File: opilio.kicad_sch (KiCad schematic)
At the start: 87 parts, among them J1 Screw_Terminal_01x02, J2 USB_B_Micro, J3 Conn_01x02_Male, J4 Conn_01x02_Male, J5 Conn_01x02_Male, Q1 PMV25ENEAR, U1 EUP3458, U2 STM32F103C8T6, Y1 YSX531SL 8MHz, Y2 YST310S 32.768KHz

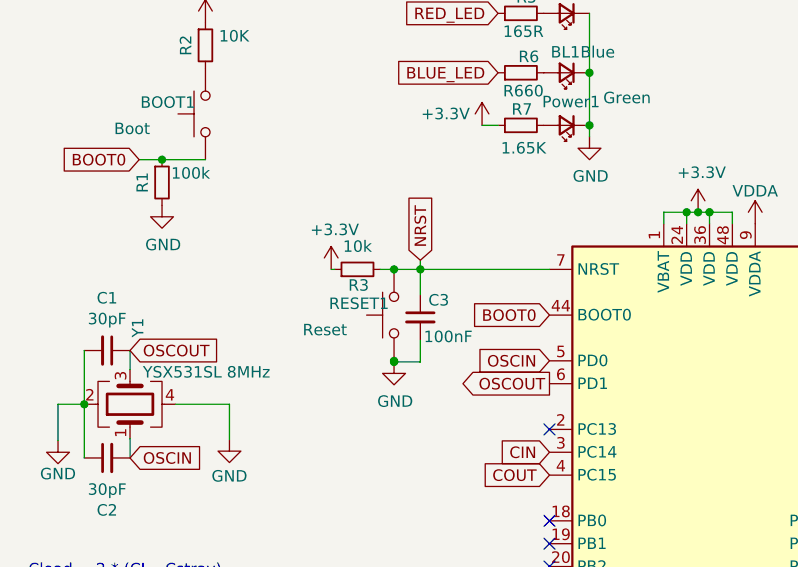
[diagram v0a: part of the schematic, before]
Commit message: bigger pads for mosfets
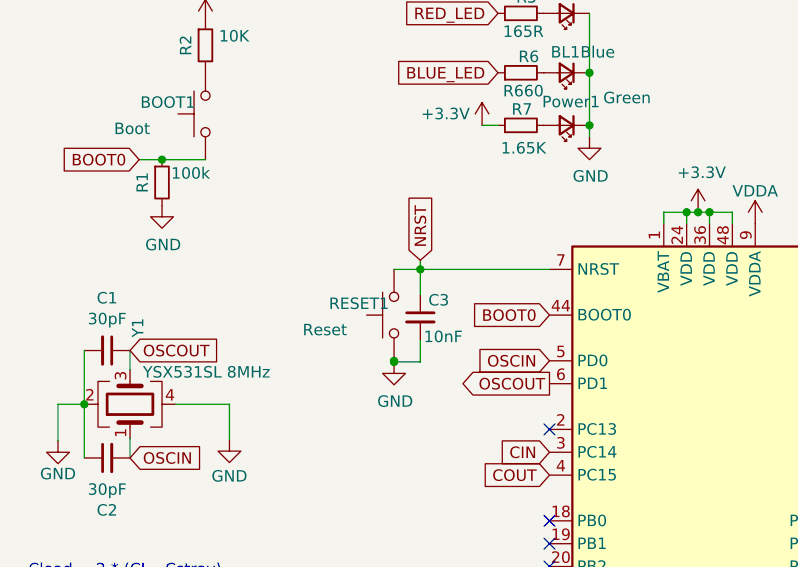
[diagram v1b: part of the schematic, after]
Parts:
- removed R3: 10k, Resistor_SMD:R_0603_1608Metric_Pad0.98x0.95mm_HandSolder, symbol Device:R_Small
- C3: value 100nF -> 10nF
- Q1: footprint easyeda2kicad:SOT-23_L2.9-W1.3-P1.90-LS2.4-BR -> Package_TO_SOT_SMD:SOT-23
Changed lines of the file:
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@@
   (junction (at 88.773 112.522) (diameter 0) (color 0 0 0 0)
   )
-  (junction (at 53.721 118.872) (diameter 0) (color 0 0 0 0)
-  )
   (junction (at 17.907 166.37) (diameter 0) (color 0 0 0 0)
   )
@@
     (stroke (width 0) (type default) (color 0 0 0 0))
   )
-  (wire (pts (xy 52.197 118.872) (xy 53.721 118.872))
-    (stroke (width 0) (type default) (color 0 0 0 0))
-  )
   (wire (pts (xy 14.732 27.178) (xy 14.732 31.75))
     (stroke (width 0) (type default) (color 0 0 0 0))
@@
     (stroke (width 0) (type default) (color 0 0 0 0))
   )
-  (wire (pts (xy 46.736 118.872) (xy 47.117 118.872))
-    (stroke (width 0) (type default) (color 0 0 0 0))
-  )
   (wire (pts (xy 221.996 101.092) (xy 219.456 101.092))
     (stroke (width 0) (type default) (color 0 0 0 0))
@@
     )
   )
-  (symbol (lib_id "Device:R_Small") (at 49.657 118.872 90) (unit 1)
-    (in_bom yes) (on_board yes)
-    (property "Reference" "R3" (id 0) (at 49.784 120.65 90))
-    (property "Value" "10k" (id 1) (at 49.657 116.332 90))
-    (property "Footprint" "Resistor_SMD:R_0603_1608Metric_Pad0.98x0.95mm_HandSolder" (id 2) (at 49.657 118.872 0)
-      (effects (font (size 1.27 1.27)) hide)
-    )
-    (property "Datasheet" "~" (id 3) (at 49.657 118.872 0)
-      (effects (font (size 1.27 1.27)) hide)
-    )
-    (pin "1")
-    (pin "2")
-  )
   (symbol (lib_id "Switch:SW_Push") (at 32.766 101.6 90) (unit 1)
     (in_bom yes) (on_board yes)
@@
       (effects (font (size 1.27 1.27)) (justify left))
     )
-    (property "Value" "100nF" (id 1) (at 57.023 126.365 0)
+    (property "Value" "10nF" (id 1) (at 57.023 126.365 0)
       (effects (font (size 1.27 1.27)) (justify left))
     )
@@
       (effects (font (size 1.27 1.27)) (justify left))
     )
-    (property "Footprint" "easyeda2kicad:SOT-23_L2.9-W1.3-P1.90-LS2.4-BR" (id 2) (at 204.343 91.44 0)
+    (property "Footprint" "Package_TO_SOT_SMD:SOT-23" (id 2) (at 204.343 91.44 0)
       (effects (font (size 1.27 1.27)) hide)
     )
@@
     (pin "1")
   )
-  (symbol (lib_id "power:+3.3V") (at 46.736 118.872 0) (unit 1)
-    (in_bom yes) (on_board yes)
-    (property "Reference" "#PWR09" (id 0) (at 46.736 122.682 0)
-      (effects (font (size 1.27 1.27)) hide)
-    )
-    (property "Value" "+3.3V" (id 1) (at 47.117 114.4778 0))
-    (property "Footprint" "" (id 2) (at 46.736 118.872 0)
-      (effects (font (size 1.27 1.27)) hide)
-    )
-    (property "Datasheet" "" (id 3) (at 46.736 118.872 0)
-      (effects (font (size 1.27 1.27)) hide)
-    )
-    (pin "1")
-  )
   (symbol (lib_id "power:GND") (at 87.503 192.532 0) (unit 1)
     (in_bom yes) (on_board yes)
@@
       (reference "#PWR08") (unit 1) (value "GND") (footprint "")
     )
-    (path "/fcdd5368-7d46-4e3b-b033-9204303556cd"
-      (reference "#PWR09") (unit 1) (value "+3.3V") (footprint "")
-    )
     (path "/53efbcf9-b8b0-41cf-b5f1-95d5ffb0f13b"
       (reference "#PWR010") (unit 1) (value "+12V") (footprint "")
@@
     )
     (path "/725ad605-0047-4399-a661-42b9902e5238"
-      (reference "C3") (unit 1) (value "100nF") (footprint "Capacitor_SMD:C_0603_1608Metric_Pad1.08x0.95mm_HandSolder")
+      (reference "C3") (unit 1) (value "10nF") (footprint "Capacitor_SMD:C_0603_1608Metric_Pad1.08x0.95mm_HandSolder")
     )
     (path "/9d3abc30-14c9-40c1-8ddc-4b7be6965203"
@@
     )
     (path "/df940eb1-429e-48e8-8206-0d27bc3ed7bd"
-      (reference "Q1") (unit 1) (value "PMV25ENEAR") (footprint "easyeda2kicad:SOT-23_L2.9-W1.3-P1.90-LS2.4-BR")
+      (reference "Q1") (unit 1) (value "PMV25ENEAR") (footprint "Package_TO_SOT_SMD:SOT-23")
     )
     (path "/be987873-4856-4ad7-aaee-745ffdc5e733"
@@
       (reference "R2") (unit 1) (value "10K") (footprint "Resistor_SMD:R_0603_1608Metric_Pad0.98x0.95mm_HandSolder")
     )
-    (path "/058aa005-48f2-4086-a77a-42a9c22cdeee"
-      (reference "R3") (unit 1) (value "10k") (footprint "Resistor_SMD:R_0603_1608Metric_Pad0.98x0.95mm_HandSolder")
-    )
     (path "/beb113ce-d7fe-47cb-97e6-be05f9ef150e"

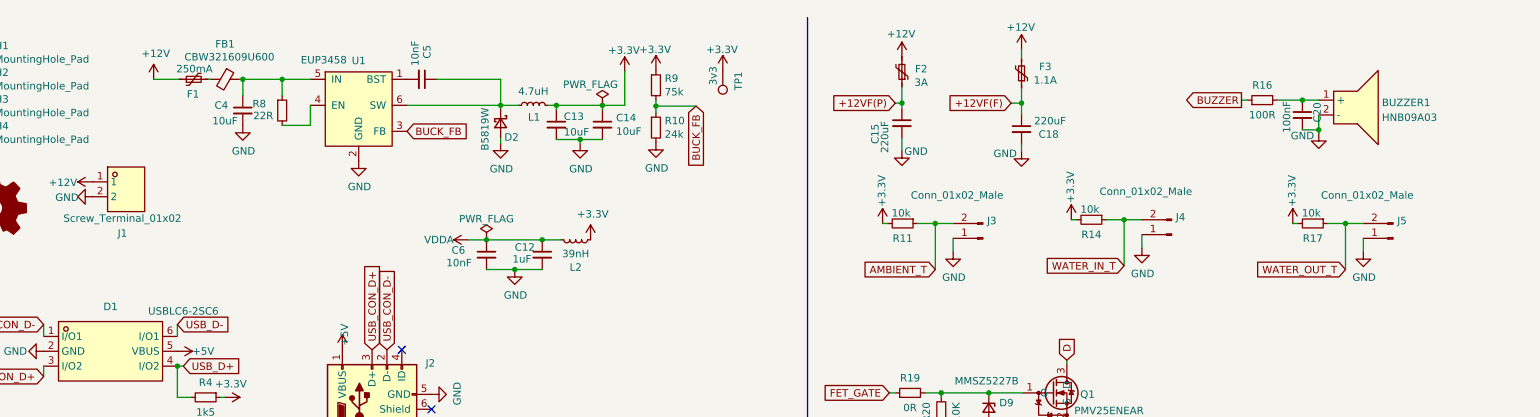
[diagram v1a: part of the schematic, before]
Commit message: added 3d models
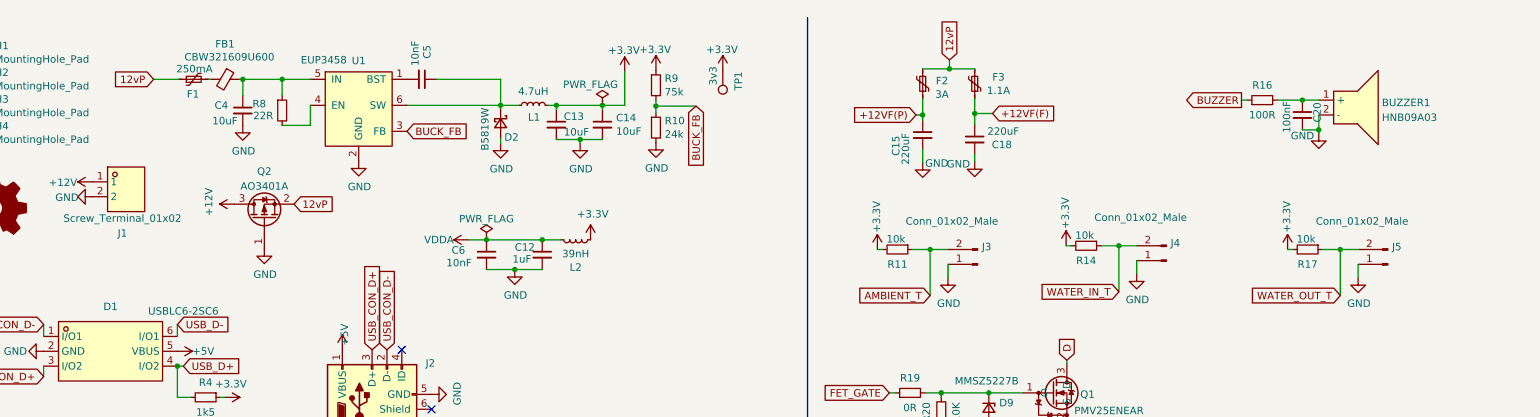
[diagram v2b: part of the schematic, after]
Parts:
- added Q2: AO3401A, Package_TO_SOT_SMD:SOT-23, symbol Transistor_FET:AO3401A
- D1: footprint easyeda2kicad:SOT-666-6_L1.6-W1.2-P0.50-LS1.6-BL -> Package_TO_SOT_SMD:SOT-666
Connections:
- net +12V: now also Q2.3 (D); no longer F1.1, F2.2, F3.2
- net GND: now also Q2.1 (G)
- new net 12vP: F1.1, F2.2, F3.2, Q2.2 (S)
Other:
- moved on the sheet: C15, C18, F2, F3, J3, J4, J5, R11, R14, R17

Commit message: cleanup and annotate schema
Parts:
- F2: value 3A -> 2A; footprint Fuse:Fuse_1812_4532Metric_Pad1.30x3.40mm_HandSolder -> Fuse:Fuse_1206_3216Metric_Pad1.42x1.75mm_HandSolder
- R20: value 10K -> 7k5
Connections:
- net USB_CON_D+: now also R4.2
- net USB_D+: no longer R4.2
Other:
- note added: "10k Thermistor Input"
- note added: "Audio/Visual Output"
- note added: "ESD Protection"
- note added: "MCU"
- note added: "N-FET"
- note added: "Power"
- note added: "Power Output"
- moved on the sheet: BL1, BUZZER1, C10, C11, C12, C15, C18, C20, C6, C7, C8, C9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

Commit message: WIP:0402
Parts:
- C1, C10, C11, C16, C17, C19, C2, C20, C21, C22, C23, C3, C6, C8, C9: footprint Capacitor_SMD:C_0603_1608Metric_Pad1.08x0.95mm_HandSolder -> Capacitor_SMD:C_0402_1005Metric_Pad0.74x0.62mm_HandSolder
- R1, R10, R11, R12, R13, R14, R15, R16, R17, R18, R2, R20, R4, R5, R6, R7, R8, R9: footprint Resistor_SMD:R_0603_1608Metric_Pad0.98x0.95mm_HandSolder -> Resistor_SMD:R_0402_1005Metric_Pad0.72x0.64mm_HandSolder

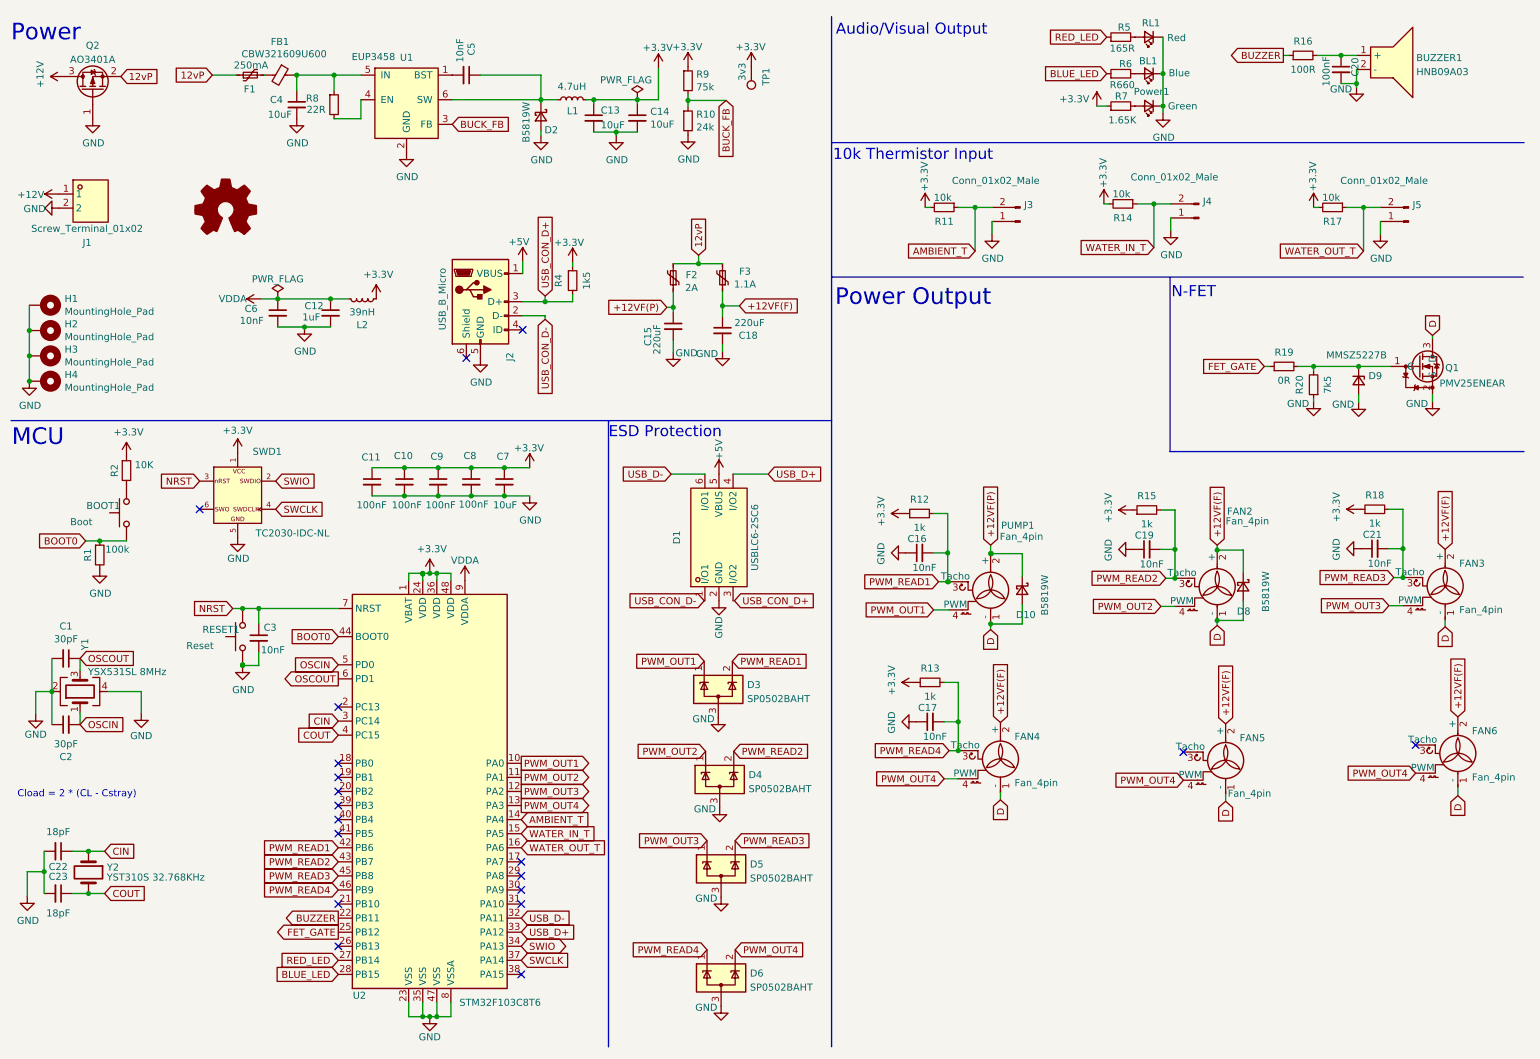
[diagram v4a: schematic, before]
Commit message: shrink board, 0402 passives
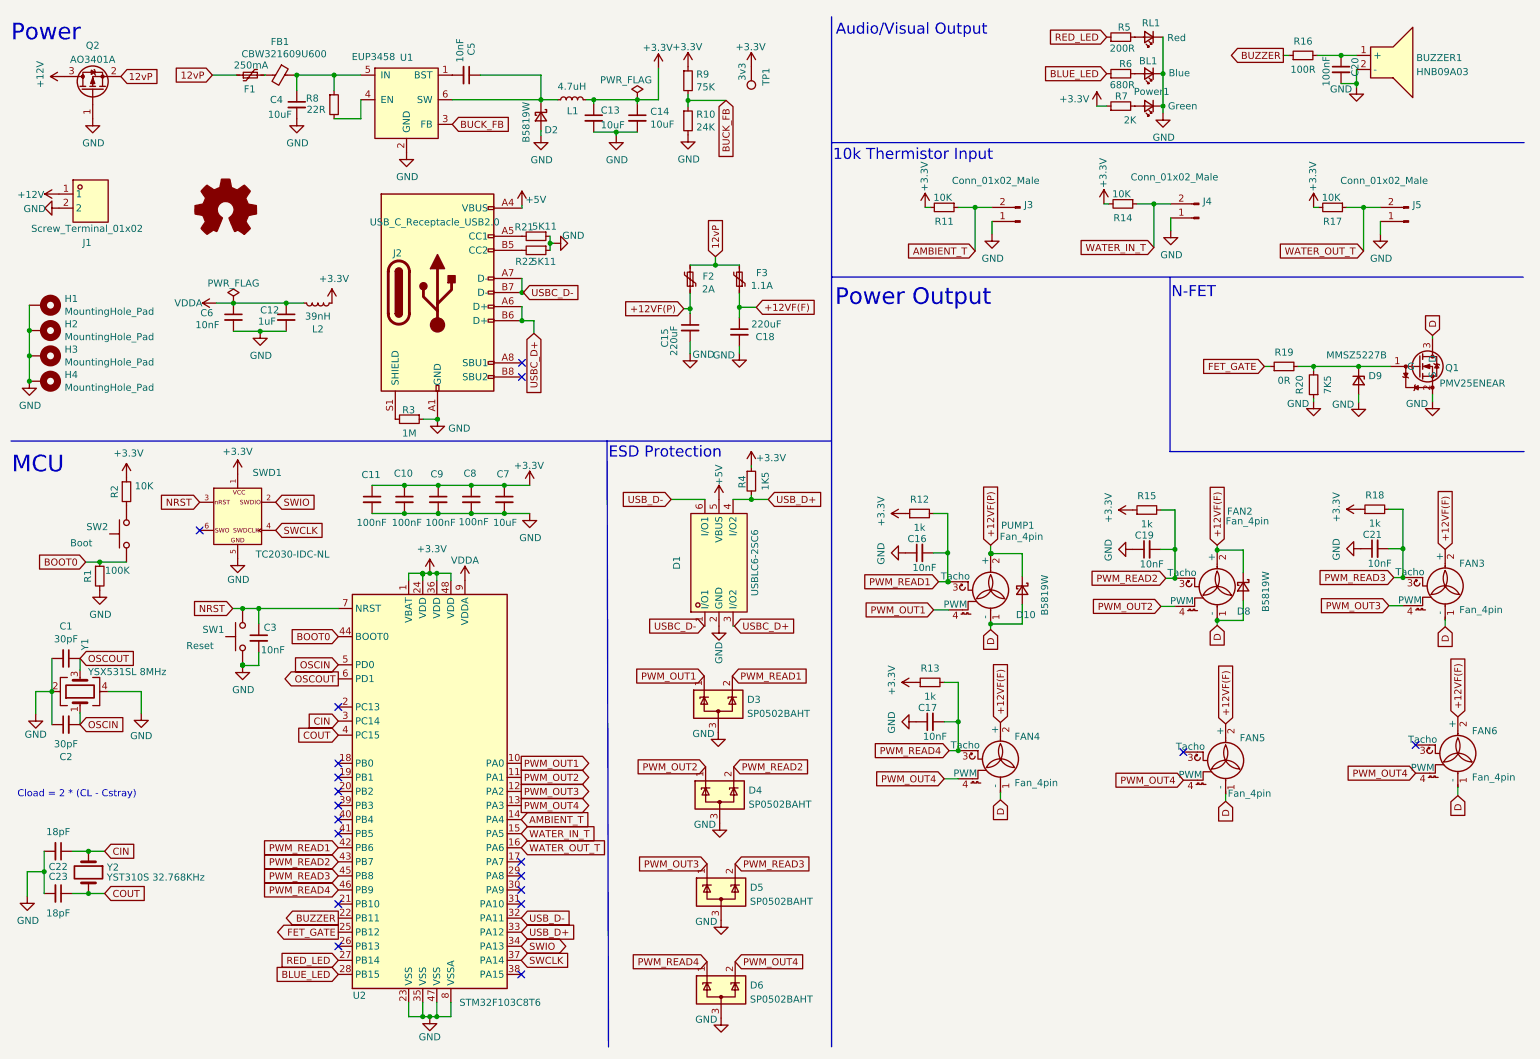
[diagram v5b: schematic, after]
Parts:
- removed J2: USB_B_Micro, Custom:USB_Micro-B_Wuerth_629105150521_narrow_holes, symbol Connector:USB_B_Micro
- added J2: USB_C_Receptacle_USB2.0, Custom:USB_C_Receptacle_Palconn_UTC16-G_Streached_pads, symbol Connector:USB_C_Receptacle_USB2.0
- added R21, R22: 5K11, Resistor_SMD:R_0402_1005Metric_Pad0.72x0.64mm_HandSolder, symbol Device:R_Small
- added R3: 1M, Resistor_SMD:R_0402_1005Metric_Pad0.72x0.64mm_HandSolder, symbol Device:R_Small
- BL1: LCSC Part (none) -> C72041
- C1, C2: LCSC Part (none) -> C458861
- C10, C11, C20, C8, C9: LCSC Part (none) -> C100072
- C12: LCSC Part (none) -> C328910
- C13, C14, C4, C7: LCSC Part (none) -> C92487
- C15, C18: LCSC Part (none) -> C696188
- C16, C17, C19, C21, C3, C6: LCSC Part (none) -> C272878
- C22, C23: LCSC Part (none) -> C33149
- C5: footprint Capacitor_SMD:C_0603_1608Metric_Pad1.08x0.95mm_HandSolder -> Capacitor_SMD:C_0402_1005Metric_Pad0.74x0.62mm_HandSolder; LCSC Part (none) -> C272878
- D10, D2, D8: LCSC Part (none) -> C917036
- D3, D4, D5, D6: LCSC Part (none) -> C70435
- D9: LCSC Part (none) -> C2903820
- F1: LCSC Part (none) -> C269112
- F2: LCSC Part (none) -> C883135
- F3: LCSC Part (none) -> C883130
- FAN2, FAN3, FAN4, FAN5, FAN6, H1, H2, H3, H4, J3, J4, J5, LOGO1, PUMP1, SWD1, TP1: LCSC Part (none) -> NA
- FB1: LCSC Part (none) -> C73732
- L1: LCSC Part (none) -> C405113
- L2: LCSC Part (none) -> C578032
- Power1: LCSC Part (none) -> C479607
- Q2: LCSC Part (none) -> C15127; Manufacturer (none) -> Alpha & Omega Semicon
- R1: value 100k -> 100K; LCSC Part (none) -> C144809
- R10: value 24k -> 24K; LCSC Part (none) -> C2984415
- R11, R14, R17: value 10k -> 10K; LCSC Part (none) -> C191123
- R12, R13, R15, R18: LCSC Part (none) -> C144789
- R16: LCSC Part (none) -> C106232
- R19: footprint Resistor_SMD:R_0603_1608Metric_Pad0.98x0.95mm_HandSolder -> Resistor_SMD:R_0402_1005Metric_Pad0.72x0.64mm_HandSolder; LCSC Part (none) -> C396825
- R2: LCSC Part (none) -> C191123
- R20: value 7k5 -> 7K5; LCSC Part (none) -> C137934
- R4: value 1k5 -> 1K5; LCSC Part (none) -> C144792
- R5: value 165R -> 200R; LCSC Part (none) -> C114764
- R6: value R660 -> 680R; LCSC Part (none) -> C100510
- R7: value 1.65K -> 2K; LCSC Part (none) -> C137887
- R8: LCSC Part (none) -> C226359
- R9: value 75k -> 75K; LCSC Part (none) -> C2689478
- RL1: LCSC Part (none) -> C1322295
- SW1: renamed from RESET1; footprint easyeda2kicad:SW-SMD_L6.0-W3.3-LS8.0 -> easyeda2kicad:SW-SMD_L3.0-W2.5-P3.40-LS4.0-L; LCSC Part (none) -> C2689695
- SW2: renamed from BOOT1; footprint easyeda2kicad:SW-SMD_L6.0-W3.3-LS8.0 -> easyeda2kicad:SW-SMD_L3.0-W2.5-P3.40-LS4.0-L; LCSC Part (none) -> C2689695
- U1: LCSC Part (none) -> C89300
- U2: LCSC Part (none) -> C8734
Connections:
- net +5V: now also J2.A4 (VBUS), J2.A9 (VBUS), J2.B4 (VBUS), J2.B9 (VBUS)
- net GND: now also J2.A1 (GND), J2.A12 (GND), J2.B1 (GND), J2.B12 (GND), R21.1, R22.1, R3.1
- net USB_D+: now also R4.2
- net USB_CON_D+ renamed USBC_D+
- net USBC_D+: now also J2.A6 (D+), J2.B6 (D+); no longer R4.2
- net USB_CON_D- renamed USBC_D-
- net USBC_D-: now also J2.A7 (D-), J2.B7 (D-)
- new net: J2.B5 (CC2), R22.2
- new net: J2.S1 (SHIELD), R3.2
- new net: J2.A5 (CC1), R21.2
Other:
- moved on the sheet: C10, C11, C12, C15, C18, C6, C7, C8, C9, D1, D3, D4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

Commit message: built
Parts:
- D10, D8: footprint Diode_SMD:D_SOD-123 -> Diode_SMD:D_SMA-SMB_Universal_Handsoldering
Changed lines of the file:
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@@
       (effects (font (size 1.27 1.27)) (justify left))
     )
-    (property "Footprint" "Diode_SMD:D_SOD-123" (id 2) (at 194.437 115.57 90)
+    (property "Footprint" "Diode_SMD:D_SMA-SMB_Universal_Handsoldering" (id 2) (at 194.437 115.57 90)
       (effects (font (size 1.27 1.27)) hide)
     )
@@
       (effects (font (size 1.27 1.27)) (justify left))
     )
-    (property "Footprint" "Diode_SMD:D_SOD-123" (id 2) (at 234.315 114.935 90)
+    (property "Footprint" "Diode_SMD:D_SMA-SMB_Universal_Handsoldering" (id 2) (at 234.315 114.935 90)
       (effects (font (size 1.27 1.27)) hide)
     )
@@
     )
     (path "/5cb7e9de-3e66-4610-a2af-946e934b4121"
-      (reference "D8") (unit 1) (value "B5819W") (footprint "Diode_SMD:D_SOD-123")
+      (reference "D8") (unit 1) (value "B5819W") (footprint "Diode_SMD:D_SMA-SMB_Universal_Handsoldering")
     )
     (path "/e88626b9-3fe1-48ae-acbd-a97bcfa3f3b1"
@@
     )
     (path "/236fa9cf-d5fd-47ef-b78b-d2577b8c8ed8"
-      (reference "D10") (unit 1) (value "B5819W") (footprint "Diode_SMD:D_SOD-123")
+      (reference "D10") (unit 1) (value "B5819W") (footprint "Diode_SMD:D_SMA-SMB_Universal_Handsoldering")
     )
     (path "/1dbe0b67-5506-4ac5-862b-00a8669b4e81"
